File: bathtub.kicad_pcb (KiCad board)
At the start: 2 copper layers, 91.4 x 71.1 mm, 29 parts, among them J1 Screw_Terminal_01x03 - Hot wa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, J2 Screw_Terminal_01x03 - Cold w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, J3 Screw_Terminal_01x02, J4 Screw_Terminal_01x03 - Inputs, J5 Barrel_Jack, Q1 2N2219, Q2 2N2219, SW1 SW_Push, SW2 SW_Push

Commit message: feat: version 1.  Sent out for review
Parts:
- removed F1: Slow Blow Fuse - 1.5A, Fuse:Fuseholder_Littelfuse_100_series_5x20mm
- removed PS1: IH2405S, Converter_DCDC:Converter_DCDC_XP_POWER-IHxxxxS_THT
- added F1 - 1.5A: Slow Blow Fuse - 1.5A, Fuse:Fuseholder_Littelfuse_100_series_5x20mm, F.Cu at (119.3, 95.2)
- added R10: .01, Resistor_THT:R_Axial_DIN0207_L6.3mm_D2.5mm_P2.54mm_Vertical, F.Cu at (152.7, 74.7)
- added U1: L7805CV, Package_TO_SOT_THT:TO-220-3_Vertical, F.Cu at (147.3, 85.1)
- A1: moved to B.Cu
- C1, C2: value 0.1uF -> 0.01uF
- J1: value Screw_Terminal_01x03 - Hot water -> Screw_Terminal_01x03
- J2: value Screw_Terminal_01x03 - Cold water -> Screw_Terminal_01x03
- J3: value Screw_Terminal_01x02 -> Terminal_01x02
- J4: value Screw_Terminal_01x03 - Inputs -> Terminal 01x03 - Inputs
- R1, R2: value 250 ohms -> 250
- R3, R6: value 200ohm -> 200
- R4, R5: value 100ohm -> 220
- moved A1 80.5 mm to (156.5, 52.8)
- moved D1 72.4 mm to (119.4, 57.1), turned to 0 degrees
- moved J5 69.5 mm to (111.7, 96.5), turned to -90 degrees
- moved R1 56.1 mm to (134.6, 72.4)
- moved Q1 53.4 mm to (124.5, 64.8)
- moved J2 48.3 mm to (108.7, 73.6)
- moved R5 45.2 mm to (119.4, 116.6)
- moved C1 40.1 mm to (116.8, 64.8)
- moved C3 37.1 mm to (149.9, 92.7)
- moved R7 35.9 mm to (167.6, 90.2), turned to -90 degrees
- moved C4 35.2 mm to (160.0, 92.7)
- moved R3 33.6 mm to (149.9, 109.0), turned to 90 degrees
- moved Q2 31.7 mm to (124.5, 77.5)
- moved R4 30.4 mm to (139.7, 114.0), turned to 0 degrees
- moved R8 29.5 mm to (150.6, 67.3)
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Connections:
- net +5V renamed +12V
- A1 pad 20: Net-(A1-Pad20) -> unconnected-(A1-Pad20)
- A1 pad 21: Net-(A1-Pad21) -> unconnected-(A1-Pad21)
- A1 pad 24: unconnected-(A1-Pad24) -> Net-(A1-Pad24)
- A1 pad 27: unconnected-(A1-Pad27) -> Net-(A1-Pad27)
- A1 pad 29: -5V -> GND
- A1 pad 30: unconnected-(A1-Pad30) -> Net-(A1-Pad30)
- A1 pad 6: -5V -> GND
- A1 pad 7: -5V -> GND
- C1 pad 2: -24V -> GND
- C2 pad 1: Net-(C2-Pad1) -> Net-(D2-Pad2)
- C2 pad 2: -24V -> GND
- C3 pad 2: -24V -> GND
- C4 pad 2: -5V -> GND
- D1 pad 1: Net-(D1-Pad1) -> +24V
- D2 pad 1: Net-(D2-Pad1) -> +24V
- D2 pad 2: Net-(C2-Pad1) -> Net-(D2-Pad2)
- D3 pad 1: -5V -> GND
- D4 pad 1: -5V -> GND
- J1 pad 1: unconnected-(J1-Pad1) -> +24V
- J1 pad 2: unconnected-(J1-Pad2) -> Net-(C1-Pad1)
- J1 pad 3: -24V -> GND
- J2 pad 1: unconnected-(J2-Pad1) -> +24V
- J2 pad 2: unconnected-(J2-Pad2) -> Net-(D2-Pad2)
- J2 pad 3: -24V -> GND
- J3 pad 1: unconnected-(J3-Pad1) -> Net-(J3-Pad1)
- J3 pad 2: unconnected-(J3-Pad2) -> Net-(A1-Pad5)
- J4 pad 1: unconnected-(J4-Pad1) -> Net-(J4-Pad1)
- J4 pad 3: unconnected-(J4-Pad3) -> Net-(J4-Pad3)
- J5 pad 2: -24V -> GND
- Q1 pad 1: Net-(D1-Pad1) -> GND
- Q1 pad 3: +24V -> Net-(C1-Pad1)
- Q2 pad 1: Net-(D2-Pad1) -> GND
- Q2 pad 3: +24V -> Net-(D2-Pad2)
- R1 pad 1: Net-(Q1-Pad2) -> Net-(A1-Pad28)
- R1 pad 2: Net-(A1-Pad21) -> Net-(Q1-Pad2)
- R2 pad 1: Net-(Q2-Pad2) -> Net-(A1-Pad27)
- R2 pad 2: Net-(A1-Pad17) -> Net-(Q2-Pad2)
- R3 pad 1: -5V -> Net-(R3-Pad1)
- R3 pad 2: Net-(A1-Pad28) -> GND
- R6 pad 1: -5V -> Net-(R6-Pad1)
- R6 pad 2: Net-(A1-Pad23) -> GND
- R7 pad 1: unconnected-(R7-Pad1) -> Net-(J3-Pad1)
- R7 pad 2: Net-(A1-Pad20) -> Net-(A1-Pad17)
- R9 pad 1: unconnected-(R9-Pad1) -> Net-(J4-Pad3)
- R9 pad 2: -5V -> GND
- SW1 pad 1: Net-(A1-Pad5) -> Net-(R3-Pad1)
- SW2 pad 1: Net-(A1-Pad5) -> Net-(R6-Pad1)
- SW2 pad 2: Net-(A1-Pad28) -> Net-(A1-Pad24)
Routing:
- net Net-(D2-Pad2): track 0.00 -> 56.7 mm
- net Net-(A1-Pad27): track 0.00 -> 45.3 mm
- net Net-(A1-Pad30): track 0.00 -> 44.5 mm
- net Net-(A1-Pad5): track 0.00 -> 44.2 mm
- net Net-(R3-Pad1): track 0.00 -> 42.4 mm
- net -5V: track 38.1 -> 0.00 mm
- net Net-(A1-Pad17): track 9.68 -> 45.1 mm
- net Net-(D1-Pad1): track 34.1 -> 0.00 mm
- net Net-(A1-Pad28): track 9.05 -> 41.8 mm
- net Net-(C1-Pad1): track 0.00 -> 32.7 mm
- net Net-(Q2-Pad2): track 36.8 -> 8.67 mm
- net Net-(A1-Pad9): track 0.00 -> 25.5 mm
- net Net-(Q1-Pad2): track 30.0 -> 8.67 mm
- net Net-(A1-Pad23): track 13.5 -> 34.7 mm
- net Net-(D2-Pad1): track 20.5 -> 0.00 mm
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- added copper zone on B.Cu, net GND
- added copper zone on F.Cu, net GND
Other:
- board size 91.4 x 71.1 mm -> 76.2 x 71.1 mm
- board text added: "5V"
- board text added: "GND"

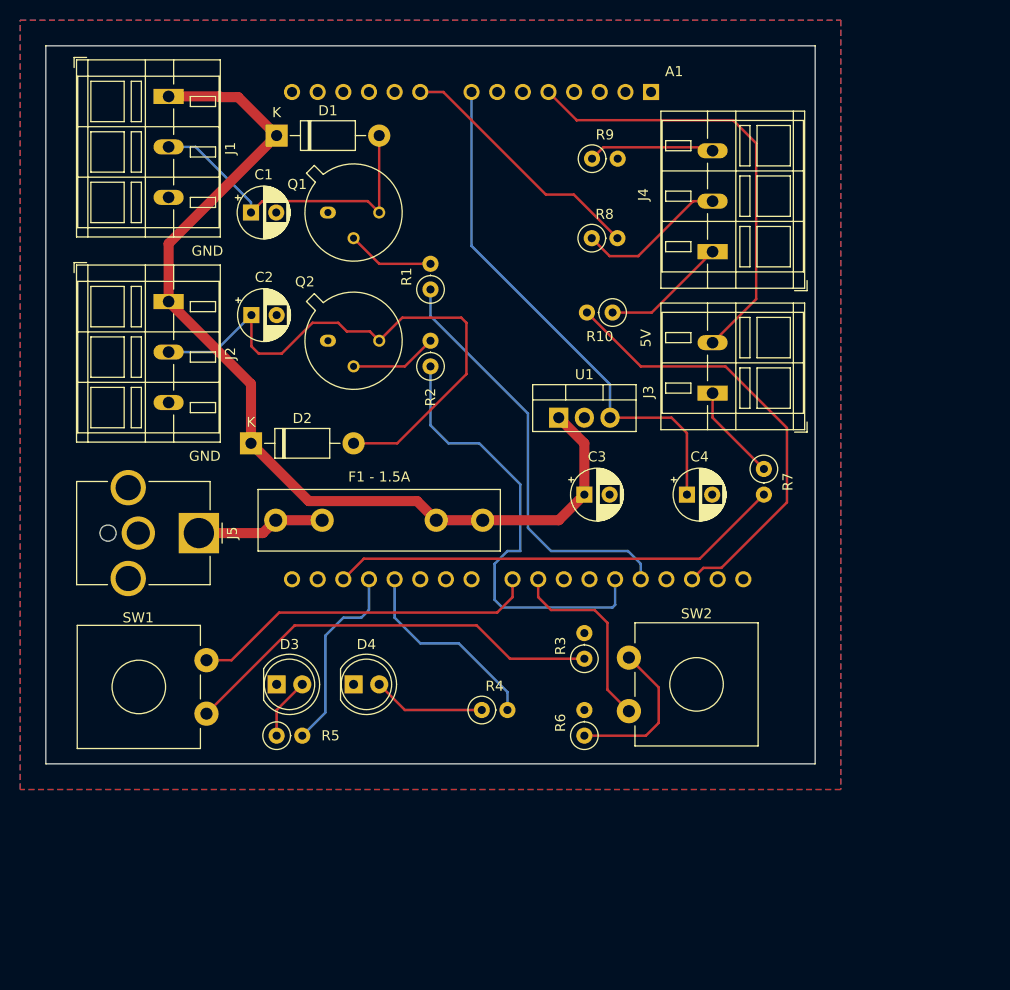
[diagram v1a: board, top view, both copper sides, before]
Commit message: fix: small tweaks Added pull down resistors for the inputs
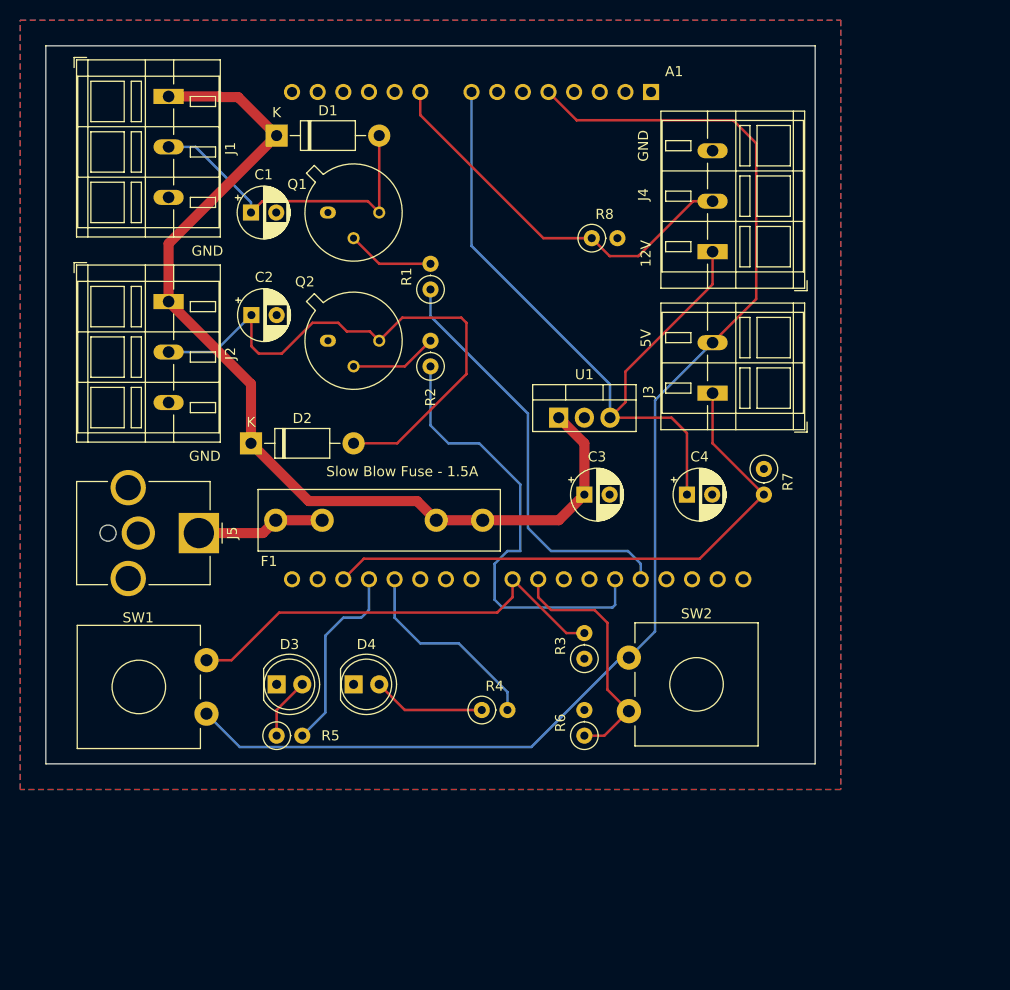
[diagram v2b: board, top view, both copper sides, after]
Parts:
- removed R10, R9: .01, Resistor_THT:R_Axial_DIN0207_L6.3mm_D2.5mm_P2.54mm_Vertical
- C3: value 0.33uF -> 10uF
- C4: value 0.1uF -> 22uF
- F1: renamed from F1 - 1.5A
- J3: value Terminal_01x02 -> Screw_Terminal_01x02
- J4: value Terminal 01x03 - Inputs -> Screw_Terminal_01x03 - Inputs
- R1, R2: value 250 -> 365
- R3, R6: value 200 -> 10k
- R7: value .01 -> 10k
- R8: value .01 -> 250
- U1: value L7805CV -> N7812-1C
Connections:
- A1 pad 30: Net-(A1-Pad30) -> unconnected-(A1-Pad30)
- A1 pad 5: Net-(A1-Pad5) -> +5V
- A1 pad 9: Net-(A1-Pad9) -> Net-(J4-Pad2)
- J3 pad 1: Net-(J3-Pad1) -> Net-(A1-Pad17)
- J3 pad 2: Net-(A1-Pad5) -> +5V
- J4 pad 1: Net-(J4-Pad1) -> +12V
- J4 pad 3: Net-(J4-Pad3) -> GND
- R3 pad 1: Net-(R3-Pad1) -> GND
- R3 pad 2: GND -> Net-(A1-Pad23)
- R6 pad 1: Net-(R6-Pad1) -> Net-(A1-Pad24)
- R7 pad 1: Net-(J3-Pad1) -> GND
- R8 pad 2: Net-(A1-Pad9) -> GND
- SW1 pad 1: Net-(R3-Pad1) -> +5V
- SW2 pad 1: Net-(R6-Pad1) -> +5V
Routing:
- net +5V: track 0.00 -> 125.7 mm
- net Net-(A1-Pad30): track 44.5 -> 0.00 mm
- net Net-(A1-Pad5): track 44.2 -> 0.00 mm
- net Net-(R3-Pad1): track 42.4 -> 0.00 mm
- net Net-(A1-Pad9): track 25.5 -> 0.00 mm
- net Net-(J4-Pad2): track 15.0 -> 39.3 mm
- net +12V: track 52.3 -> 72.9 mm
- net Net-(R6-Pad1): track 15.6 -> 0.00 mm
- net Net-(J4-Pad3): track 12.5 -> 0.00 mm
- net Net-(J4-Pad1): track 12.4 -> 0.00 mm
- net Net-(A1-Pad17): track 45.1 -> 57.3 mm
- net Net-(J3-Pad1): track 9.61 -> 0.00 mm
- net Net-(A1-Pad23): track 34.7 -> 44.0 mm
- net Net-(A1-Pad24): track 19.3 -> 24.7 mm
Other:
- board text added: "12V"

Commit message: fix: moved meanwell and increased trace size J2 has the updated footprint, while J1 has the old Haven't updated the PCB yet
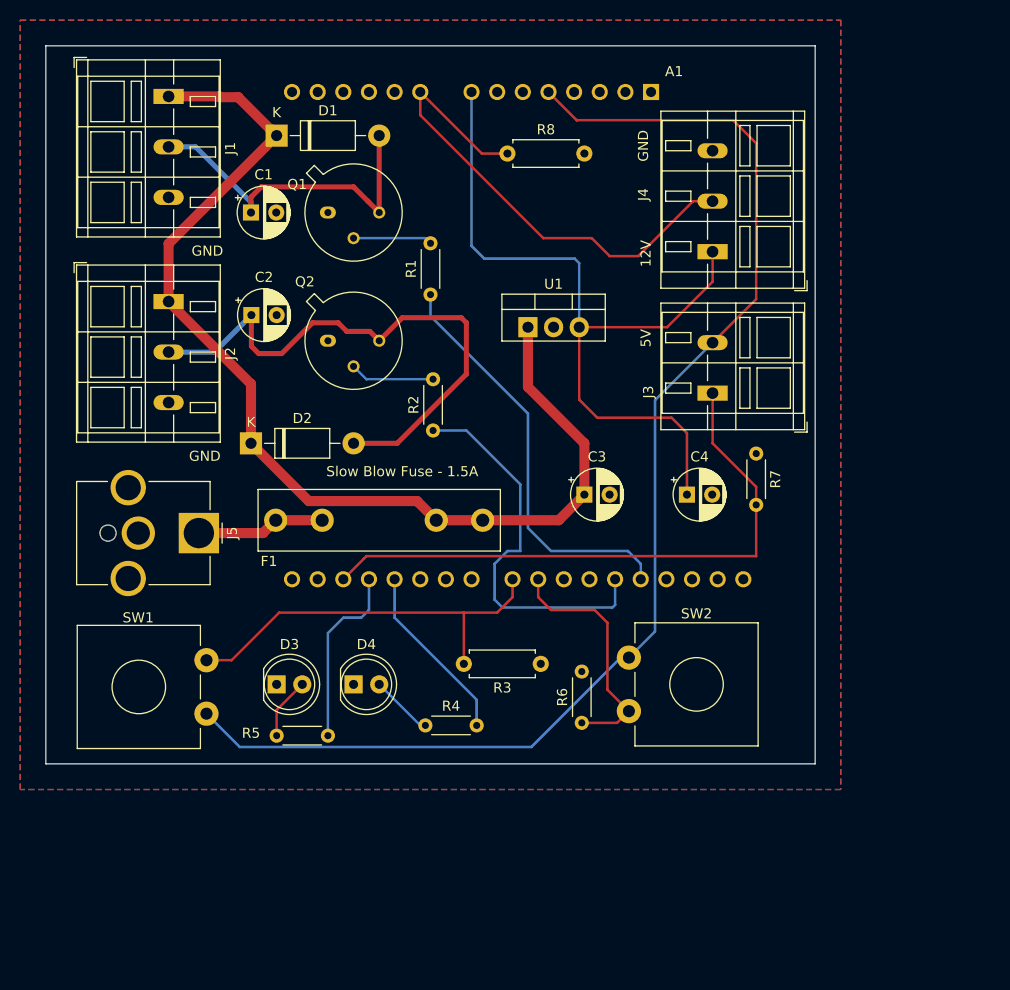
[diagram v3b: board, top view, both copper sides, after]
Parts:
- R1, R2, R4, R5, R6, R7: footprint Resistor_THT:R_Axial_DIN0207_L6.3mm_D2.5mm_P2.54mm_Vertical -> Resistor_THT:R_Axial_DIN0204_L3.6mm_D1.6mm_P5.08mm_Horizontal
- R3, R8: footprint Resistor_THT:R_Axial_DIN0207_L6.3mm_D2.5mm_P2.54mm_Vertical -> Resistor_THT:R_Axial_DIN0207_L6.3mm_D2.5mm_P7.62mm_Horizontal
- moved R8 11.8 mm to (142.2, 58.9)
- moved U1 9.47 mm to (144.3, 76.1)
- moved R2 6.36 mm to (134.9, 86.4)
- moved R4 5.79 mm to (134.1, 115.6)
- moved R3 4.35 mm to (145.5, 109.5), turned to 180 degrees
- moved R7 1.70 mm to (166.9, 88.6)
- moved R6 1.30 mm to (149.6, 115.3)
- moved R1 0.51 mm to (134.6, 72.9)
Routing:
- net Net-(A1-Pad9): track 39.3 -> 50.4 mm
- net +24V: track 96.5 -> 106.7 mm
- net Net-(A1-Pad27): track 45.3 -> 39.0 mm
- net Net-(D4-Pad2): track 11.2 -> 6.26 mm
- net Net-(A1-Pad23): track 44.0 -> 39.8 mm
- net +12V: track 72.9 -> 76.3 mm
- net Net-(A1-Pad17): track 57.3 -> 59.8 mm
- net Net-(C1-Pad1): track 32.7 -> 34.8 mm
- net Net-(A1-Pad19): track 19.8 -> 17.8 mm
- net Net-(A1-Pad18): track 19.3 -> 18.2 mm
- net Net-(Q1-Pad2): track 8.67 -> 7.83 mm
- net Net-(A1-Pad28): track 41.8 -> 41.3 mm

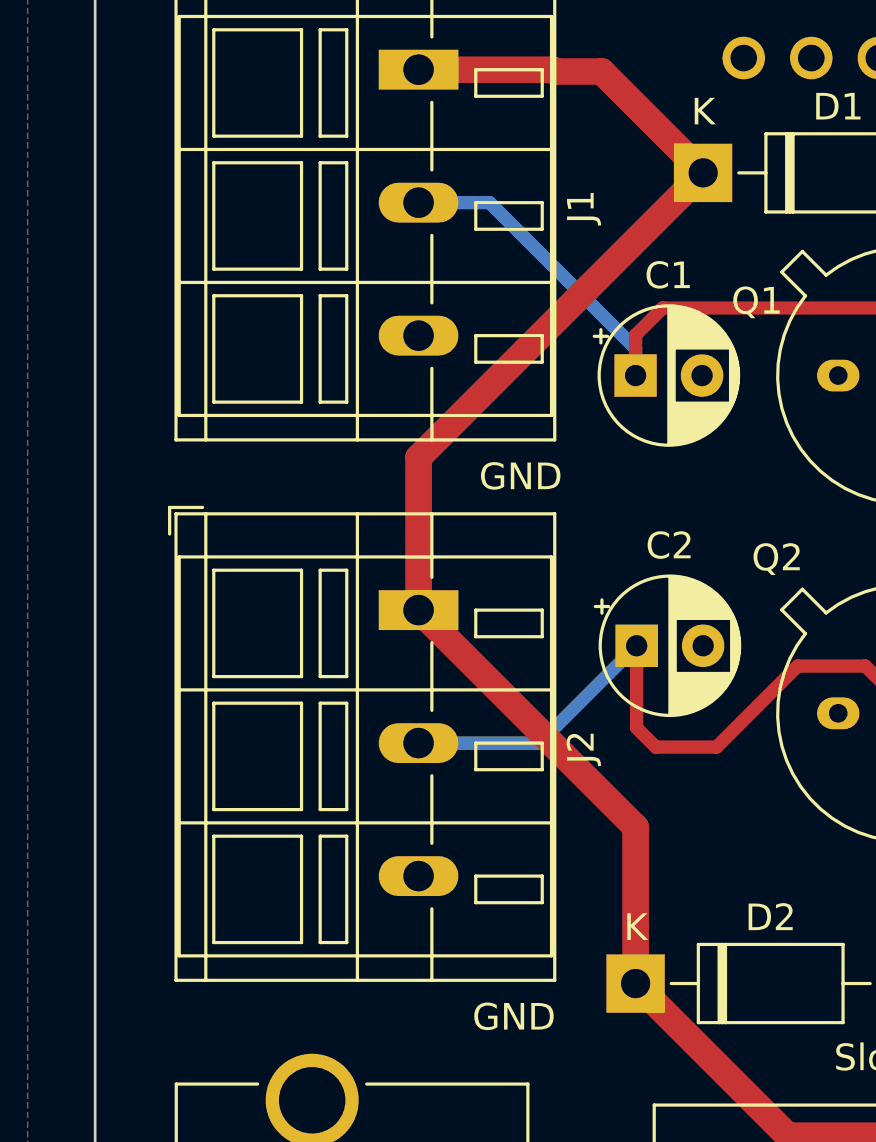
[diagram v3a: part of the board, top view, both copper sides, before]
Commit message: chore: replaced J2 with the new footprint Still need to check if its available, etc
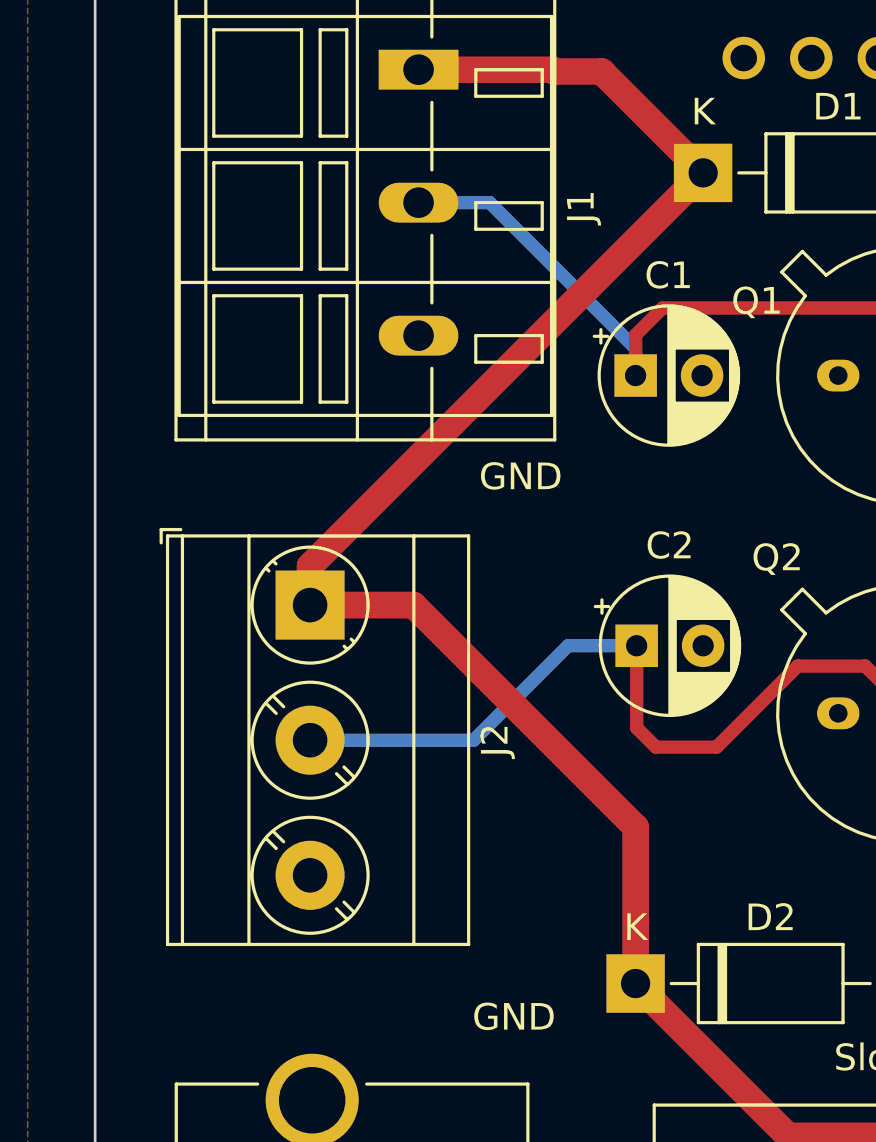
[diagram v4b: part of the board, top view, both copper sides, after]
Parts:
- J2: footprint TerminalBlock_WAGO:TerminalBlock_WAGO_236-103_1x03_P5.00mm_45Degree -> TerminalBlock_Phoenix:TerminalBlock_Phoenix_MKDS-3-3-5.08_1x03_P5.08mm_Horizontal
- moved J2 4.08 mm to (104.6, 73.4)
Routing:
- net +24V: track 106.7 -> 112.4 mm
- net Net-(C2-Pad1): track 56.7 -> 60.7 mm
